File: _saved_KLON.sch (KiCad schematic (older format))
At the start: 69 parts, among them IC1 MAX1044ESA+, J1 Conn_01x03, J2 Conn_01x03, J3 Conn_01x02, SW1 3PDT, U1 TL072, U2 TL072

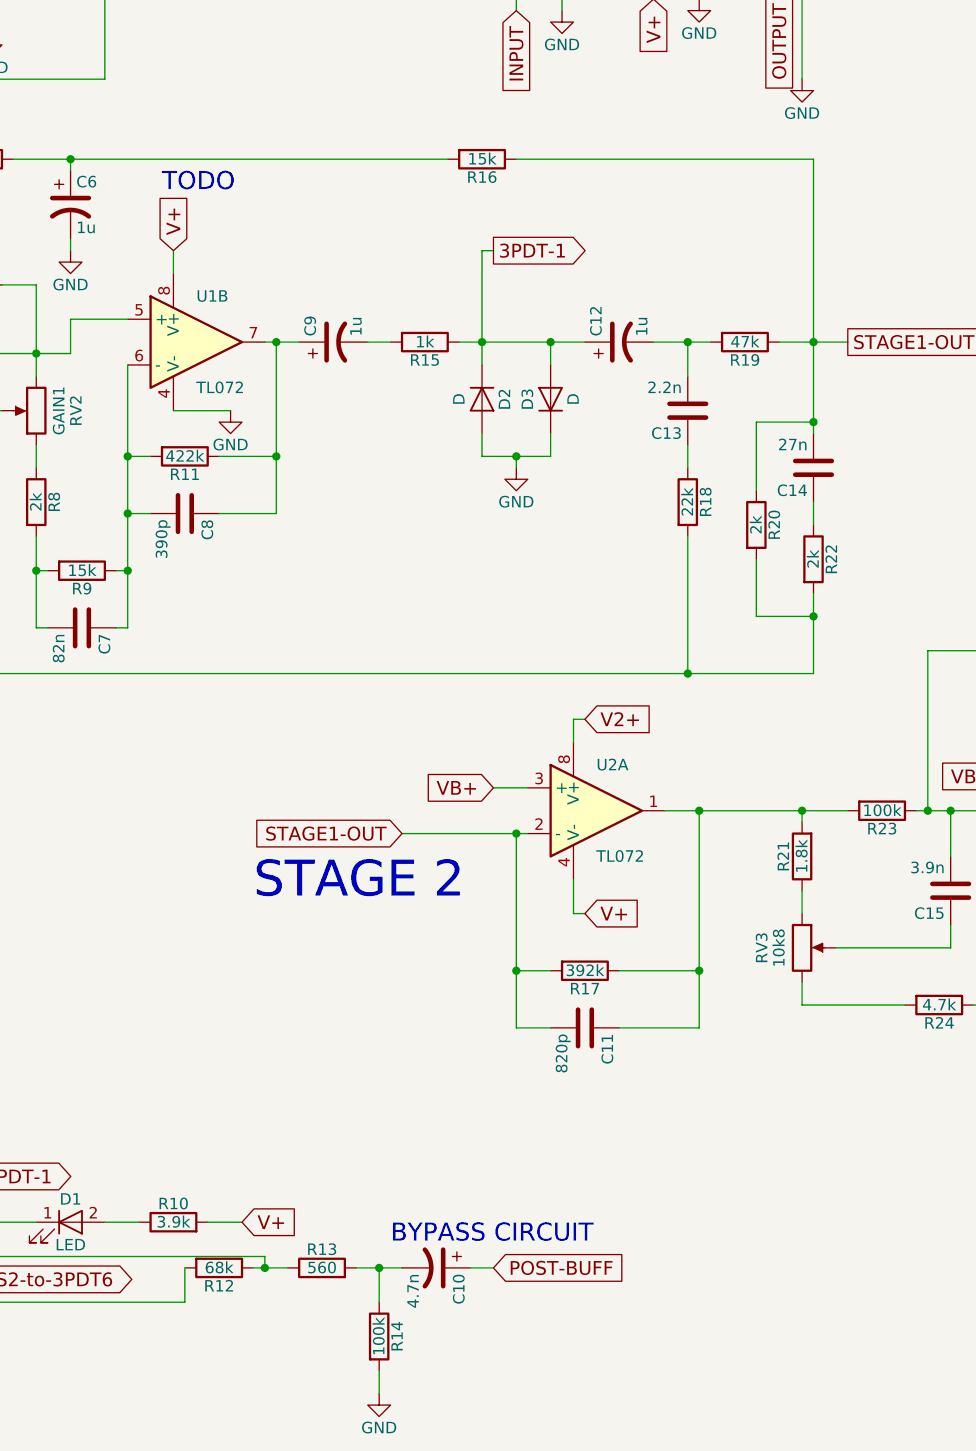
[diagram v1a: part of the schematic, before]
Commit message: added Capacitor Footprints to CSV, added capacitors to digikey BOM (will put link or .xlsx file here later)
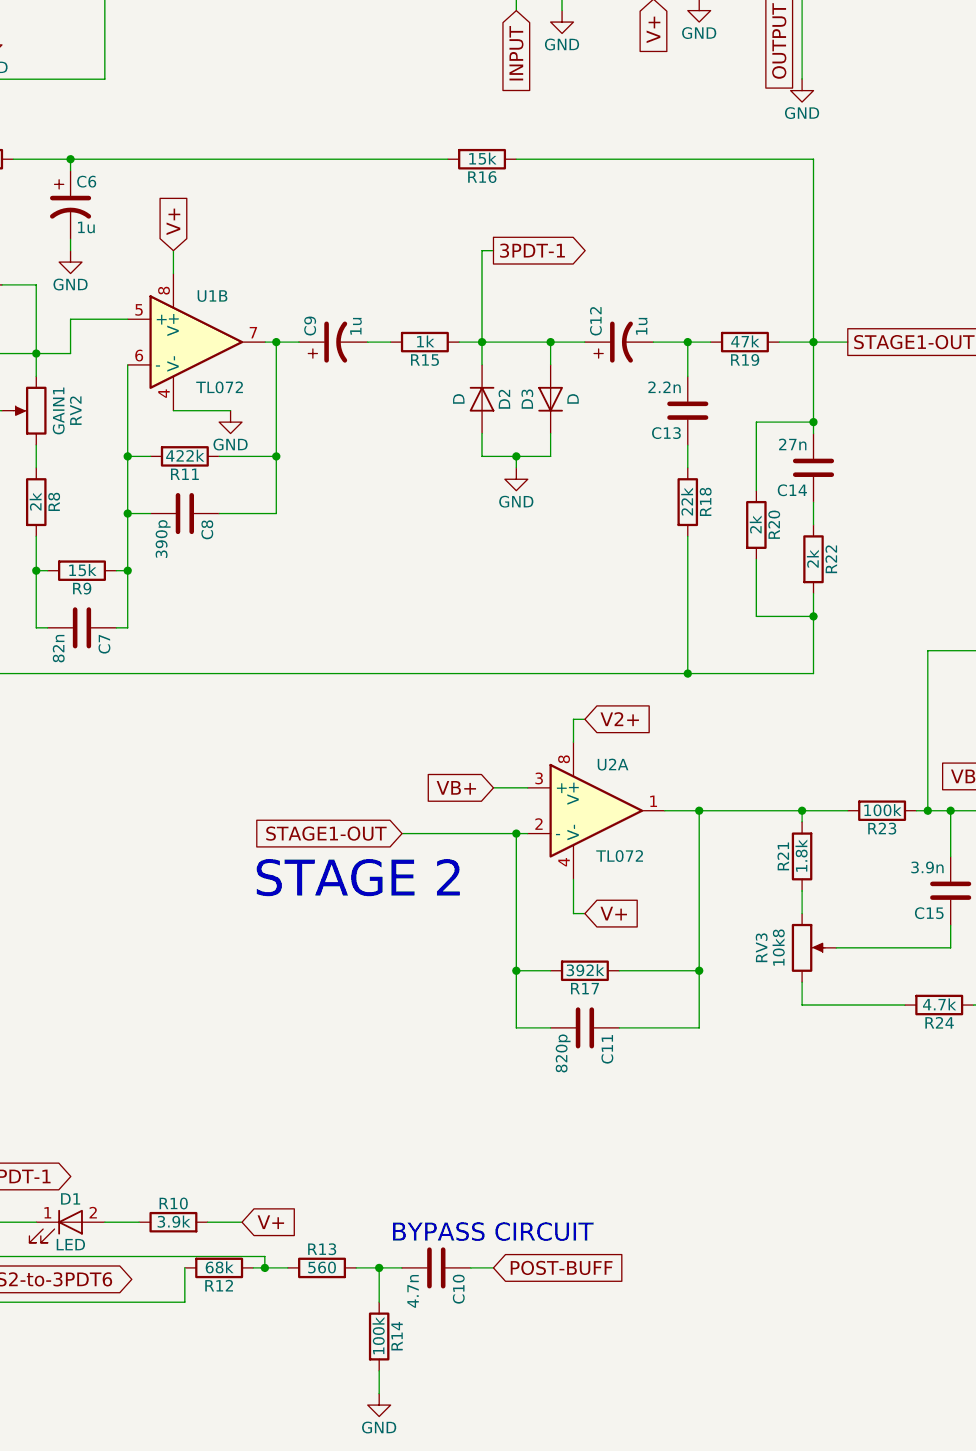
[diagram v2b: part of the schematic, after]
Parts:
- removed C10: 4.7n, Capacitors_THT:C_Rect_L7.0mm_W2.0mm_P5.00mm, symbol CP1
- added C10: 4.7n, Capacitors_THT:C_Disc_D3.8mm_W2.6mm_P2.50mm, symbol C
- C1, C2, C4: footprint Capacitors_THT:C_Rect_L7.0mm_W2.5mm_P5.00mm -> Capacitors_THT:C_Rect_L10.3mm_W5.7mm_P7.50mm_MKS4
- C11, C8: footprint Capacitors_THT:C_Rect_L7.0mm_W2.5mm_P5.00mm -> Capacitors_THT:C_Rect_L4.0mm_W2.5mm_P2.50mm
- C12, C16, C17, C19, C20, C22, C6, C9: footprint Capacitors_THT:CP_Radial_D5.0mm_P2.00mm -> Capacitors_THT:CP_Radial_D5.0mm_P2.50mm
- C13, C14, C15: footprint Capacitors_THT:C_Rect_L7.0mm_W2.0mm_P5.00mm -> Capacitors_THT:C_Disc_D3.8mm_W2.6mm_P2.50mm
- C18, C21: footprint Capacitors_THT:CP_Radial_D5.0mm_P2.00mm -> Capacitors_THT:CP_Radial_D6.3mm_P2.50mm
- C3, C5: footprint Capacitors_THT:C_Rect_L7.0mm_W2.5mm_P5.00mm -> Capacitors_THT:C_Disc_D6.0mm_W2.5mm_P5.00mm
- C7: footprint Capacitors_THT:C_Rect_L7.0mm_W2.0mm_P5.00mm -> Capacitors_THT:C_Rect_L4.0mm_W2.5mm_P2.50mm
- IC1: footprint SOIC127P600X175-8N -> Housings_DIP:DIP-8_W7.62mm_Socket
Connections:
- net POST-BUFF: now also C10.1
- net at R13.2, R14.1: now also C10.2
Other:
- note removed: "TODO"
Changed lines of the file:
@@
 F 0 "C1" H 1725 800 50  0000 L CNN
 F 1 ".1u" H 1725 600 50  0000 L CNN
-F 2 "Capacitors_THT:C_Rect_L7.0mm_W2.5mm_P5.00mm" H 1738 550 50  0001 C CNN
+F 2 "Capacitors_THT:C_Rect_L10.3mm_W5.7mm_P7.50mm_MKS4" H 1738 550 50  0001 C CNN
 F 3 "" H 1700 700 50  0001 C CNN
 	1    1700 700
@@
 F 0 "C2" H 1725 2800 50  0000 L CNN
 F 1 ".1u" H 1725 2600 50  0000 L CNN
-F 2 "Capacitors_THT:C_Rect_L7.0mm_W2.5mm_P5.00mm" H 1738 2550 50  0001 C CNN
+F 2 "Capacitors_THT:C_Rect_L10.3mm_W5.7mm_P7.50mm_MKS4" H 1738 2550 50  0001 C CNN
 F 3 "" H 1700 2700 50  0001 C CNN
 	1    1700 2700
@@
 F 0 "C3" H 1725 3400 50  0000 L CNN
 F 1 "68n" H 1725 3200 50  0000 L CNN
-F 2 "Capacitors_THT:C_Rect_L7.0mm_W2.5mm_P5.00mm" H 1738 3150 50  0001 C CNN
+F 2 "Capacitors_THT:C_Disc_D6.0mm_W2.5mm_P5.00mm" H 1738 3150 50  0001 C CNN
 F 3 "" H 1700 3300 50  0001 C CNN
 	1    1700 3300
@@
 F 0 "C4" H 1725 4000 50  0000 L CNN
 F 1 ".39u" H 1725 3800 50  0000 L CNN
-F 2 "Capacitors_THT:C_Rect_L7.0mm_W2.5mm_P5.00mm" H 1738 3750 50  0001 C CNN
+F 2 "Capacitors_THT:C_Rect_L10.3mm_W5.7mm_P7.50mm_MKS4" H 1738 3750 50  0001 C CNN
 F 3 "" H 1700 3900 50  0001 C CNN
 	1    1700 3900
@@
 F 0 "C5" H 2375 2500 50  0000 L CNN
 F 1 "68n" H 2375 2300 50  0000 L CNN
-F 2 "Capacitors_THT:C_Rect_L7.0mm_W2.5mm_P5.00mm" H 2388 2250 50  0001 C CNN
+F 2 "Capacitors_THT:C_Disc_D6.0mm_W2.5mm_P5.00mm" H 2388 2250 50  0001 C CNN
 F 3 "" H 2350 2400 50  0001 C CNN
 	1    2350 2400
@@
 F 0 "C7" H 2875 4000 50  0000 L CNN
 F 1 "82n" H 2875 3800 50  0000 L CNN
-F 2 "Capacitors_THT:C_Rect_L7.0mm_W2.0mm_P5.00mm" H 2888 3750 50  0001 C CNN
+F 2 "Capacitors_THT:C_Rect_L4.0mm_W2.5mm_P2.50mm" H 2888 3750 50  0001 C CNN
 F 3 "" H 2850 3900 50  0001 C CNN
 	1    2850 3900
@@
 F 0 "C8" H 3325 3500 50  0000 L CNN
 F 1 "390p" H 3325 3300 50  0000 L CNN
-F 2 "Capacitors_THT:C_Rect_L7.0mm_W2.5mm_P5.00mm" H 3338 3250 50  0001 C CNN
+F 2 "Capacitors_THT:C_Rect_L4.0mm_W2.5mm_P2.50mm" H 3338 3250 50  0001 C CNN
 F 3 "" H 3300 3400 50  0001 C CNN
 	1    3300 3400
@@
 F 0 "C6" H 2825 2150 50  0000 L CNN
 F 1 "1u" H 2825 1950 50  0000 L CNN
-F 2 "Capacitors_THT:CP_Radial_D5.0mm_P2.00mm" H 2800 2050 50  0001 C CNN
+F 2 "Capacitors_THT:CP_Radial_D5.0mm_P2.50mm" H 2800 2050 50  0001 C CNN
 F 3 "" H 2800 2050 50  0001 C CNN
 	1    2800 2050
@@
 F 0 "C9" H 3975 2750 50  0000 L CNN
 F 1 "1u" H 3975 2550 50  0000 L CNN
-F 2 "Capacitors_THT:CP_Radial_D5.0mm_P2.00mm" H 3950 2650 50  0001 C CNN
+F 2 "Capacitors_THT:CP_Radial_D5.0mm_P2.50mm" H 3950 2650 50  0001 C CNN
 F 3 "" H 3950 2650 50  0001 C CNN
 	1    3950 2650
@@
 	0    1    1    0
 $EndComp
-Text Notes 3200 2000 0    79   ~ 0
-TODO
 $Comp
 L D D2
@@
 F 0 "C12" H 5225 2750 50  0000 L CNN
 F 1 "1u" H 5225 2550 50  0000 L CNN
-F 2 "Capacitors_THT:CP_Radial_D5.0mm_P2.00mm" H 5200 2650 50  0001 C CNN
+F 2 "Capacitors_THT:CP_Radial_D5.0mm_P2.50mm" H 5200 2650 50  0001 C CNN
 F 3 "" H 5200 2650 50  0001 C CNN
 	1    5200 2650
@@
 F 0 "C13" H 5525 3050 50  0000 L CNN
 F 1 "2.2n" H 5525 2850 50  0000 L CNN
-F 2 "Capacitors_THT:C_Rect_L7.0mm_W2.0mm_P5.00mm" H 5538 2800 50  0001 C CNN
+F 2 "Capacitors_THT:C_Disc_D3.8mm_W2.6mm_P2.50mm" H 5538 2800 50  0001 C CNN
 F 3 "" H 5500 2950 50  0001 C CNN
 	1    5500 2950
@@
 F 0 "C14" H 6075 3300 50  0000 L CNN
 F 1 "27n" H 6075 3100 50  0000 L CNN
-F 2 "Capacitors_THT:C_Rect_L7.0mm_W2.0mm_P5.00mm" H 6088 3050 50  0001 C CNN
+F 2 "Capacitors_THT:C_Disc_D3.8mm_W2.6mm_P2.50mm" H 6088 3050 50  0001 C CNN
 F 3 "" H 6050 3200 50  0001 C CNN
 	1    6050 3200
@@
 F 0 "C11" H 5075 5750 50  0000 L CNN
 F 1 "820p" H 5075 5550 50  0000 L CNN
-F 2 "Capacitors_THT:C_Rect_L7.0mm_W2.5mm_P5.00mm" H 5088 5500 50  0001 C CNN
+F 2 "Capacitors_THT:C_Rect_L4.0mm_W2.5mm_P2.50mm" H 5088 5500 50  0001 C CNN
 F 3 "" H 5050 5650 50  0001 C CNN
 	1    5050 5650
@@
 F 0 "C15" H 6675 5150 50  0000 L CNN
 F 1 "3.9n" H 6675 4950 50  0000 L CNN
-F 2 "Capacitors_THT:C_Rect_L7.0mm_W2.0mm_P5.00mm" H 6688 4900 50  0001 C CNN
+F 2 "Capacitors_THT:C_Disc_D3.8mm_W2.6mm_P2.50mm" H 6688 4900 50  0001 C CNN
 F 3 "" H 6650 5050 50  0001 C CNN
 	1    6650 5050
@@
 	5800 3300 5800 3000
 Wire Wire Line
-	5800 3000 6050 3000
+	6050 3000 5800 3000
 Connection ~ 6050 3000
 Wire Wire Line
@@
 F 0 "C19" H 8025 4750 50  0000 L CNN
 F 1 "4.7u" H 8025 4550 50  0000 L CNN
-F 2 "Capacitors_THT:CP_Radial_D5.0mm_P2.00mm" H 8000 4650 50  0001 C CNN
+F 2 "Capacitors_THT:CP_Radial_D5.0mm_P2.50mm" H 8000 4650 50  0001 C CNN
 F 3 "" H 8000 4650 50  0001 C CNN
 	1    8000 4650
@@
 POST-BUFF
 $Comp
-L CP1 C10
-U 1 1 5AB70457
-P 4400 6700
-F 0 "C10" H 4425 6800 50  0000 L CNN
-F 1 "4.7n" H 4425 6600 50  0000 L CNN
-F 2 "Capacitors_THT:C_Rect_L7.0mm_W2.0mm_P5.00mm" H 4400 6700 50  0001 C CNN
-F 3 "" H 4400 6700 50  0001 C CNN
-	1    4400 6700
-	0    1    1    0
-$EndComp
-$Comp
 L R R14
 U 1 1 5AB7084F
@@
 $EndComp
 Wire Wire Line
-	3750 6700 3600 6700
+	3600 6700 3750 6700
 Wire Wire Line
 	3650 6700 3650 6650
@@
 F 0 "IC1" H 9200 2050 50  0000 L CNN
 F 1 "MAX1044ESA+" H 9000 1950 50  0000 L CNN
-F 2 "SOIC127P600X175-8N" H 9650 1900 50  0001 L CNN
+F 2 "Housings_DIP:DIP-8_W7.62mm_Socket" H 9650 1900 50  0001 L CNN
 F 3 "http://datasheets.maximintegrated.com/en/ds/ICL7660-MAX1044.pdf" H 9650 1800 50  0001 L CNN
 F 4 "Charge Pump Switched Cap 20mA 5V" H 9650 1700 50  0001 L CNN "Description"
@@
 F 0 "C22" H 9925 2450 50  0000 L CNN
 F 1 "1u" H 9925 2250 50  0000 L CNN
-F 2 "Capacitors_THT:CP_Radial_D5.0mm_P2.00mm" H 9900 2350 50  0001 C CNN
+F 2 "Capacitors_THT:CP_Radial_D5.0mm_P2.50mm" H 9900 2350 50  0001 C CNN
 F 3 "" H 9900 2350 50  0001 C CNN
 	1    9900 2350
@@
 F 0 "C20" H 8275 2150 50  0000 L CNN
 F 1 "1u" H 8275 1950 50  0000 L CNN
-F 2 "Capacitors_THT:CP_Radial_D5.0mm_P2.00mm" H 8250 2050 50  0001 C CNN
+F 2 "Capacitors_THT:CP_Radial_D5.0mm_P2.50mm" H 8250 2050 50  0001 C CNN
 F 3 "" H 8250 2050 50  0001 C CNN
 	1    8250 2050
@@
 F 0 "C17" H 7925 2000 50  0000 L CNN
 F 1 "1u" H 7925 1800 50  0000 L CNN
-F 2 "Capacitors_THT:CP_Radial_D5.0mm_P2.00mm" H 7900 1900 50  0001 C CNN
+F 2 "Capacitors_THT:CP_Radial_D5.0mm_P2.50mm" H 7900 1900 50  0001 C CNN
 F 3 "" H 7900 1900 50  0001 C CNN
 	1    7900 1900
@@
 F 0 "C16" H 7075 2050 50  0000 L CNN
 F 1 "1u" H 7075 1850 50  0000 L CNN
-F 2 "Capacitors_THT:CP_Radial_D5.0mm_P2.00mm" H 7050 1950 50  0001 C CNN
+F 2 "Capacitors_THT:CP_Radial_D5.0mm_P2.50mm" H 7050 1950 50  0001 C CNN
 F 3 "" H 7050 1950 50  0001 C CNN
 	1    7050 1950
@@
 F 0 "C18" H 8025 1000 50  0000 L CNN
 F 1 "47u" H 8025 800 50  0000 L CNN
-F 2 "Capacitors_THT:CP_Radial_D5.0mm_P2.00mm" H 8000 900 50  0001 C CNN
+F 2 "Capacitors_THT:CP_Radial_D6.3mm_P2.50mm" H 8000 900 50  0001 C CNN
 F 3 "" H 8000 900 50  0001 C CNN
 	1    8000 900
@@
 F 0 "C21" H 9875 1200 50  0000 L CNN
 F 1 "47u" H 9875 1000 50  0000 L CNN
-F 2 "Capacitors_THT:CP_Radial_D5.0mm_P2.00mm" H 9850 1100 50  0001 C CNN
+F 2 "Capacitors_THT:CP_Radial_D6.3mm_P2.50mm" H 9850 1100 50  0001 C CNN
 F 3 "" H 9850 1100 50  0001 C CNN
 	1    9850 1100
@@
 Wire Wire Line
 	6000 1500 6000 1000
+$Comp
+L C C10
+U 1 1 5AE93261
+P 4400 6700
+F 0 "C10" H 4425 6800 50  0000 L CNN
+F 1 "4.7n" H 4425 6600 50  0000 L CNN
+F 2 "Capacitors_THT:C_Disc_D3.8mm_W2.6mm_P2.50mm" H 4438 6550 50  0001 C CNN
+F 3 "" H 4400 6700 50  0001 C CNN
+	1    4400 6700
+	0    1    1    0
+$EndComp
 $EndSCHEMATC
